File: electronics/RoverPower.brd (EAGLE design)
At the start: 24.4 x 31.4 mm, 19 parts, among them IC1 INA139, IC3 TINY25, J1 I2C/ISP, U2 L7805

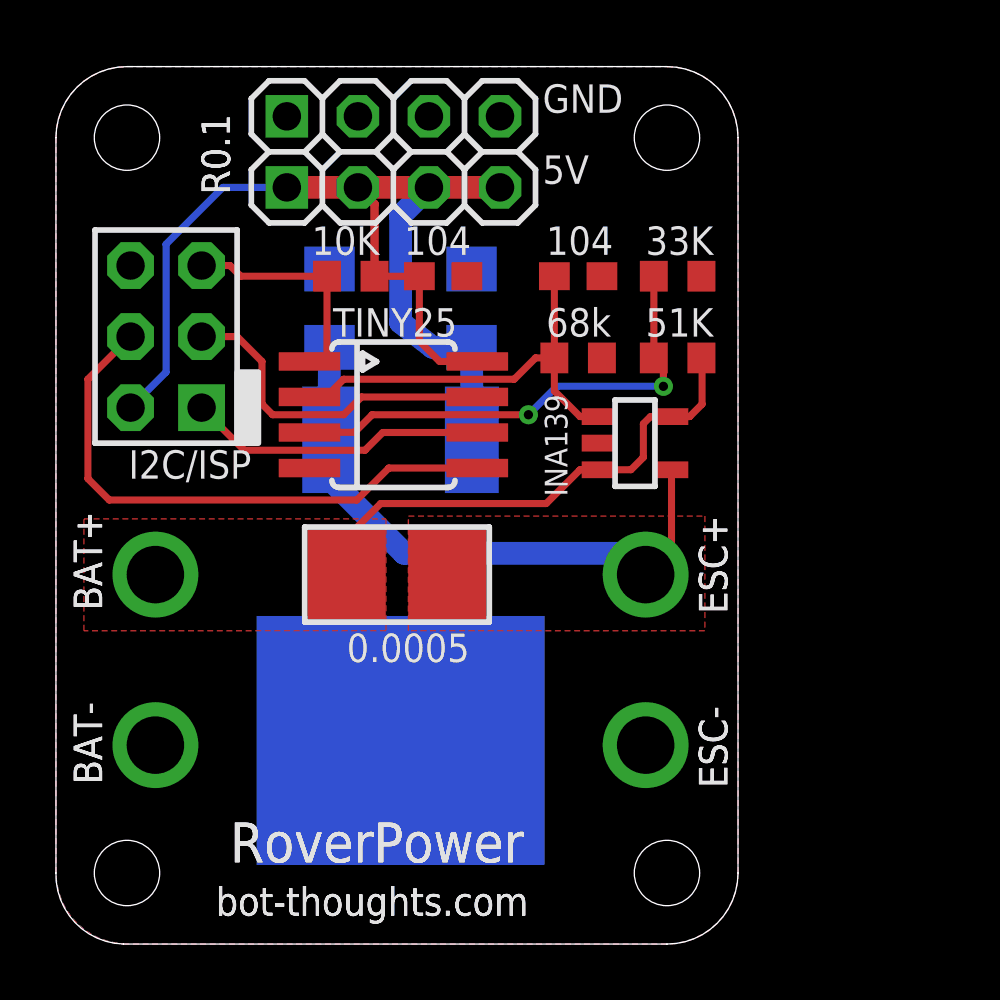
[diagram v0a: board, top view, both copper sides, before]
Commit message: Eliminated sense, added TVS and larger capacitor for input side voltage spikes, converted to LM2940 automotive regulator, replaced 10uF output cap with Tantalum 100uF, added significant thermal dissipation features, much larger traces
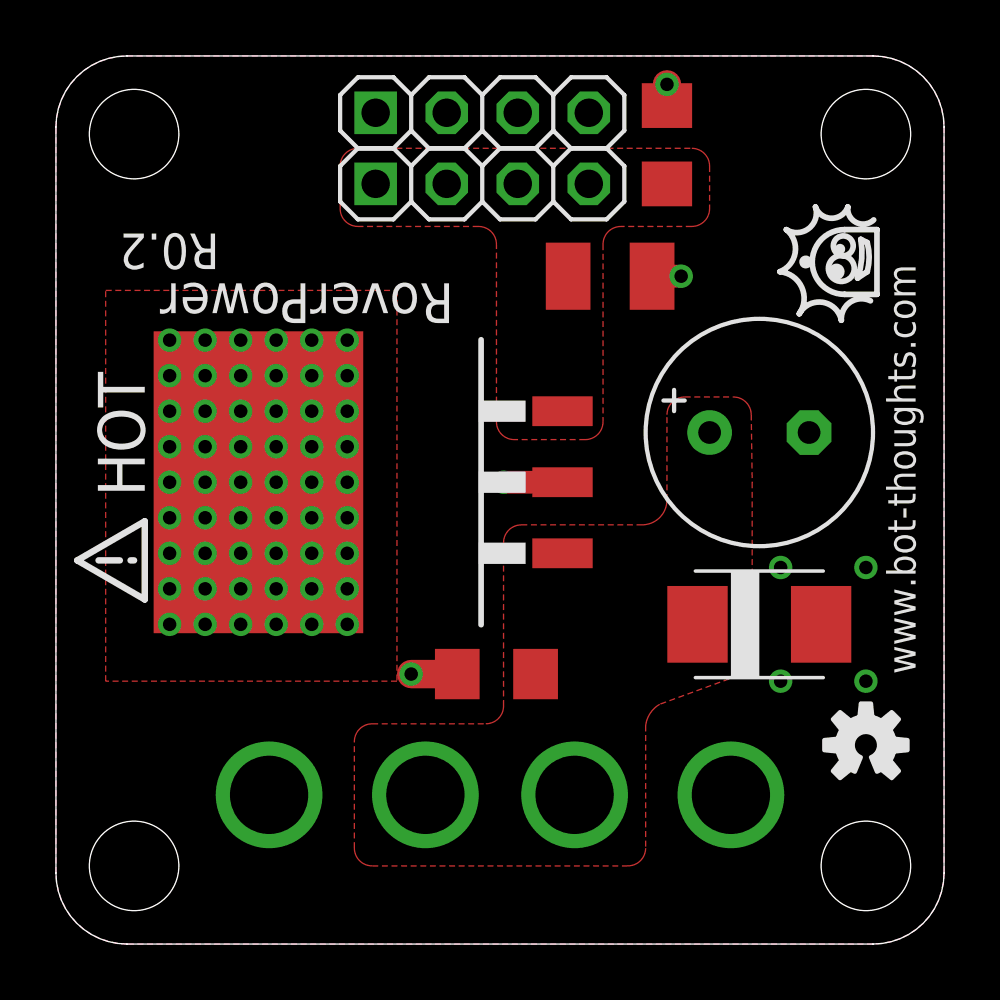
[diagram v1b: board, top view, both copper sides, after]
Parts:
- removed BAT+, BAT-, ESC+, ESC-: WIREPAD_12GA, bt_electromech:PAD_12GA
- removed IC1: INA139, burr-brown:SOT23-5
- removed IC3: TINY25, bt_avr:SOIC8
- removed J1: I2C/ISP, bt_avr:CON6P2R
- removed R1: 0.0005, bt:R2512
- removed R2: 68k, rcl:R0603
- removed R3: 51K, resistor:R0603
- removed R4: 33K, resistor:R0603
- removed R5: 10K, resistor:R0603
- removed U2: L7805, v-reg-3:D2PAK
- added D1: 13.6V, bt_diode:DO-214AA
- added JP1: VIN, bt_electromech:PAD_12GA
- added JP2, JP6: GND, bt_electromech:PAD_12GA
- added JP5: ESC, bt_electromech:PAD_12GA
- added LOGO1: OSHW-LOGOS, SparkFun-Aesthetics:OSHW-LOGO-S
- added U1: LM2940, bt_regulator:TO263-3
- C1: value 106 -> 107; device rcl:C1206 -> rcl:E3,5-8
- C3: value 104 -> 106; device resistor:C0603 -> rcl:C1206
- C4: value 104 -> 107; device rcl:C0603 -> rcl:SMC_B
- moved C1 16.0 mm to (25.1, 18.3), flipped to the top, turned to 0 degrees
- moved C2 13.1 mm to (15.7, 9.65), flipped to the top, turned to 180 degrees
- moved C4 5.97 mm to (19.8, 23.9)
- moved C3 5.67 mm to (21.8, 28.6), turned to 90 degrees
- moved JP3 3.18 mm to (15.2, 27.2)
- moved JP4 3.18 mm to (15.2, 29.7)
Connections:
- removed net !RESET: IC3.1, J1.5, R5.1
- removed net AMP: C3.1, IC1.1, IC3.2, R2.2
- removed net ESC+: C1.1, ESC+.P$1, IC1.4, R1.P$2, U2.1
- removed net MISO: IC3.6, J1.1
- removed net SCL: IC3.7, J1.3
- removed net SDA: IC3.5, J1.4
- removed net VOLT: IC3.3, R3.1, R4.2
- net 5V: now also C3.1, C4.+, U1.3; no longer C2.1, C4.1, IC3.8, J1.2, R5.2, U2.3
- net BAT+: now also C1.+, C2.1, D1.P$1, JP1.P$1, JP5.P$1, U1.1; no longer BAT+.P$1, IC1.3, IC1.5, R1.P$1, R3.2
- net GND: now also C1.-, C4.-, D1.P$2, JP2.P$1, JP6.P$1, U1.2, U1.4; no longer BAT-.P$1, C1.2, C4.2, ESC-.P$1, IC1.2, IC3.4, J1.6, R2.1, R4.1, U2.2
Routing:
- net 5V: track 40.3 -> 0.00 mm
- net ESC+: track 21.5 -> 0.00 mm
- net SDA: track 20.4 -> 0.00 mm
- net BAT+: track 18.4 -> 0.00 mm
- net VOLT: track 17.4 -> 0.00 mm, vias 2 -> 0
- net AMP: track 15.4 -> 0.00 mm
- net SCL: track 12.2 -> 0.00 mm
- net MISO: track 10.8 -> 0.00 mm
- net !RESET: track 8.30 -> 0.00 mm
- net GND: track 0.00 -> 5.56 mm, vias 0 -> 62
- added copper zone on layer 1, net 5V
- removed copper zone on layer 1, net ESC+
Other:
- board size 24.4 x 31.4 mm -> 31.8 x 31.8 mm
- board text added: "HOT"
- board text added: "R0.2"
- board text added: "www.bot-thoughts.com"
- board text removed: "#2/2mm"
- board text removed: "0.0005"
- board text removed: "104"
- board text removed: "106"
- board text removed: "10K"
- board text removed: "33K"
- board text removed: "51K"
- board text removed: "5V"
- board text removed: "68k"
- board text removed: "BAT+"
- board text removed: "BAT-"
- board text removed: "ESC+"
- board text removed: "ESC-"
- board text removed: "GND"
- board text removed: "I2C/ISP"
- board text removed: "INA139"
- board text removed: "L7805"
- board text removed: "R0.1"
- board text removed: "TINY25"
- board text removed: "bot-thoughts.com"
- board text removed: "gnd"
- board text removed: "scl"
- board text removed: "sda"
- board text removed: "vcc"

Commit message: Generated silkscreen
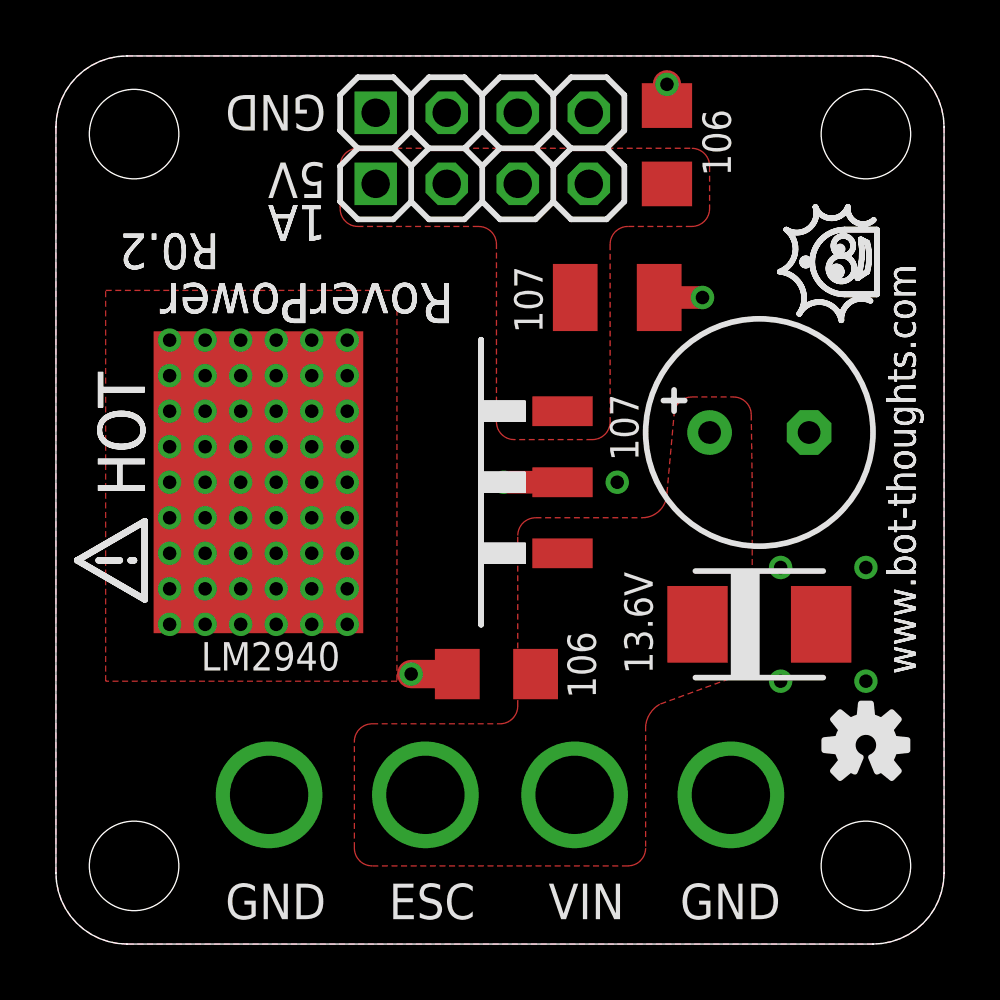
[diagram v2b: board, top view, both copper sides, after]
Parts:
- moved C4 0.80 mm to (20.1, 23.1)
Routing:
- net GND: track 5.56 -> 6.06 mm, vias 62 -> 63
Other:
- board text added: "106"
- board text added: "107"
- board text added: "13.6V"
- board text added: "1A"
- board text added: "5V"
- board text added: "ESC"
- board text added: "GND"
- board text added: "LM2940"
- board text added: "VIN"
